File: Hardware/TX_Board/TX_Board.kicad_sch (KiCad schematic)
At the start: 164 parts, among them IC1 QPA9122TR7, IC10 QPA9122TR7, IC11 QPA9122TR7, IC2 MAPS-010164-TR0500, IC3 MAPS-010164-TR0500, IC4 QPA9122TR7, IC5 GP2Y1+, IC6 GP2Y1+, IC7 GP2Y1+, IC8 MAPS-010164-TR0500, IC9 MAPS-010164-TR0500, J1 Conn_Coaxial, J2 Conn_Coaxial, J3 Conn_Coaxial, J4 Conn_Coaxial, U1 SN74HCT138NSR

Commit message: updated logic breakout and added UFL
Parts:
- added C91: 0.1uF, symbol Device:C
- added C92: 100pF, symbol Device:C
- added J5: Conn_02x08_Odd_Even, symbol Connector_Generic:Conn_02x08_Odd_Even
- added L11, L12, L4, L5, L6, L7, L8, L9: U.FL-R-SMT-1_60_, UFLRSMT160, symbol U_FL-R-SMT-1_60_:U.FL-R-SMT-1_60_
- added R48, R49, R50, R51, R52, R53, R54, R55: 0, symbol Device:R_US
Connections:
- net VCC1 is gone; now on net VCC: C38.1, C39.1, C77.1, C78.1, R19.1, R38.1
- net ATTN_LE_1: now also J5.3 (Pin_3), R50.2; no longer U1.14 (Y1)
- net ATTN_LE_2: now also J5.7 (Pin_7), R52.2; no longer U1.12 (Y3)
- net ATTN_LE_3: now also J5.11 (Pin_11), R54.2; no longer U1.10 (Y5)
- net ATTN_LE_4: now also J5.15 (Pin_15), R55.1; no longer U1.7 (Y7)
- net GND: now also C91.1, C92.1, L11.1 (GND_1), L11.2 (GND_2), L12.1 (GND_1), L12.2 (GND_2), L4.1 (GND_1), L4.2 (GND_2), L5.1 (GND_1), L5.2 (GND_2), L6.1 (GND_1), L6.2 (GND_2), L7.1 (GND_1), L7.2 (GND_2), L8.1 (GND_1), L8.2 (GND_2), L9.1 (GND_1), L9.2 (GND_2)
- net PS_LE_1: now also J5.1 (Pin_1), R49.2; no longer U1.15 (Y0)
- net PS_LE_2: now also J5.5 (Pin_5), R51.2; no longer U1.13 (Y2)
- net PS_LE_3: now also J5.9 (Pin_9), R53.2; no longer U1.11 (Y4)
- net PS_LE_4: now also J5.13 (Pin_13), R48.2; no longer U1.9 (Y6)
- net VCC: now also C91.2, C92.2
- net at C76.2, IC11.2 (RFIN): now also L11.3 (SIG)
- net at C14.2, IC1.2 (RFIN): now also L9.3 (SIG)
- net at AT.4 (RFIN), IC2.14 (RF_OUT): now also L4.3 (SIG)
- net at C37.2, IC4.2 (RFIN): now also L8.3 (SIG)
- net at AT3.4 (RFIN), IC9.14 (RF_OUT): now also L6.3 (SIG)
- net at AT2.4 (RFIN), IC8.14 (RF_OUT): now also L7.3 (SIG)
- net at AT1.4 (RFIN), IC3.14 (RF_OUT): now also L5.3 (SIG)
- net at C75.2, IC10.2 (RFIN): now also L12.3 (SIG)
- new net: R55.2, U1.7 (Y7)
- new net: R48.1, U1.9 (Y6)
- new net: R51.1, U1.13 (Y2)
- new net: R54.1, U1.10 (Y5)
- new net: R53.1, U1.11 (Y4)
- new net: R52.1, U1.12 (Y3)
- new net: R50.1, U1.14 (Y1)
- new net: R49.1, U1.15 (Y0)
- no-connect marks 0 -> 13
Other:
- moved on the sheet: AT, AT1, AT2, AT3, C11, C12, C13, C14, C15, C16, C17, C18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

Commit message: updated tx board and started layour
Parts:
- added J10, J7, J8, J9: Conn_01x01_Pin, Connector_PinHeader_2.00mm:PinHeader_1x01_P2.00mm_Vertical, symbol Connector:Conn_01x01_Pin
- added J11: Conn_Coaxial, Connector_Coaxial:SMA_Amphenol_132289_EdgeMount, symbol Connector:Conn_Coaxial
- added J12: Conn_02x04_Odd_Even, Connector_PinHeader_2.00mm:PinHeader_2x04_P2.00mm_Vertical, symbol Connector_Generic:Conn_02x04_Odd_Even
- added J6: Conn_01x03_Socket, Connector_PinSocket_2.00mm:PinSocket_1x03_P2.00mm_Vertical, symbol Connector:Conn_01x03_Socket
- added L13, L14, L15, L16: U.FL-R-SMT-1_60_, UFL_R_SMT1_1_60:UFLRSMT160, symbol U_FL-R-SMT-1_60_:U.FL-R-SMT-1_60_
- added R56, R57: 1M, Resistor_SMD:R_0402_1005Metric, symbol Device:R_US
- added U2: LDO40LPU50RY, Package_DFN_QFN:DFN-6-1EP_3x3mm_P0.95mm_EP1.7x2.6mm, symbol Regulator_Linear:LDO40LPU50RY
- added U3: ADP7182AUJZ-5.0, Package_TO_SOT_SMD:TSOT-23-5, symbol Regulator_Linear:ADP7182AUJZ-5.0
- AT1, AT2, AT3: footprint QFN50P300X300X90-17N -> RFSA3713TR7:QFN50P300X300X90-17N
- AT4: renamed from AT; footprint QFN50P300X300X90-17N -> RFSA3713TR7:QFN50P300X300X90-17N
- C1, C10, C11, C12, C13, C19, C2, C20, C21, C23, C24, C25, C26, C27, C28, C29, C3, C30, C31, C32, C33, C34, C35, C36, C4, C45, C46, C47, C48, C49, C5, C50, C51, C52, C53, C54, C55, C56, C57, C58, C59, C6, C60, C61, C62, C63, C64, C65, C66, C67, C68, C69, C7, C70, C71, C72, C73, C74, C8, C9, C91, C92: footprint (none) -> Capacitor_SMD:C_0402_1005Metric
- IC2, IC3, IC8, IC9: footprint QFN50P400X400X100-25N-D -> MAPS-010164-TR0500:QFN50P400X400X100-25N-D
- IC5, IC6, IC7: footprint QFN51P300X300X89-13N -> GP2Y1+:QFN51P300X300X89-13N
- J5: footprint (none) -> Connector_PinHeader_2.00mm:PinHeader_2x08_P2.00mm_Vertical
- L11, L12, L4, L5, L6, L7, L8, L9: footprint UFLRSMT160 -> UFL_R_SMT1_1_60:UFLRSMT160
- R1, R10, R11, R12, R13, R14, R15, R16, R17, R18, R2, R24, R25, R26, R27, R28, R29, R3, R30, R31, R32, R33, R34, R35, R36, R37, R4, R48, R49, R5, R50, R51, R52, R53, R54, R55: footprint (none) -> Resistor_SMD:R_0402_1005Metric
- U1: footprint NS16 -> SN74HCT138NSR:NS16
- renumbered C14 to C93, C17 to C94, R6 to R58
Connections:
- net ATTN_LE_1: now also J5.4 (Pin_4)
- net ATTN_LE_2: now also J5.8 (Pin_8)
- net ATTN_LE_3: now also J5.12 (Pin_12)
- net ATTN_LE_4: now also J5.16 (Pin_16)
- net GND: now also J11.2 (Ext), J6.2 (Pin_2), L13.1 (GND_1), L13.2 (GND_2), L14.1 (GND_1), L14.2 (GND_2), L15.1 (GND_1), L15.2 (GND_2), L16.1 (GND_1), L16.2 (GND_2), R56.1, R57.1, U2.1 (GND), U2.7 (GND), U3.1 (GND); no longer U1.4 (*G2A), U1.5 (*G2B)
- net GPIO0: now also J12.1 (Pin_1), J12.2 (Pin_2)
- net GPIO1: now also J12.3 (Pin_3), J12.4 (Pin_4)
- net GPIO2: now also J12.5 (Pin_5), J12.6 (Pin_6)
- net GPIO3: now also J12.7 (Pin_7), J12.8 (Pin_8)
- net PS_LE_1: now also J5.2 (Pin_2)
- net PS_LE_2: now also J5.6 (Pin_6)
- net PS_LE_3: now also J5.10 (Pin_10)
- net PS_LE_4: now also J5.14 (Pin_14)
- net RF_IN1: now also L13.3 (SIG)
- net RF_IN2: now also L14.3 (SIG)
- net RF_IN3: now also L16.3 (SIG)
- net RF_IN4: now also L15.3 (SIG)
- net VCC: now also U2.4 (Vout)
- net VEE: now also U3.5 (VOUT)
- net SDR_RF_OUT: no longer names the net of IC5.2 (SUM_PORT)
- net SDR_RF_OUT: now also J11.1 (In)
- new net: R57.2, U1.5 (*G2B)
- new net: R56.2, U1.4 (*G2A)
- new net +VDC: J6.1 (Pin_1), U2.2 (EN), U2.3 (Vin), U3.3 (EN)
- new net -VDC: J6.3 (Pin_3), U3.2 (VIN)
- no-connect marks 13 -> 5
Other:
- moved on the sheet: AT1, AT2, AT3, AT4, C1, C10, C11, C12, C13, C14, C15, C16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

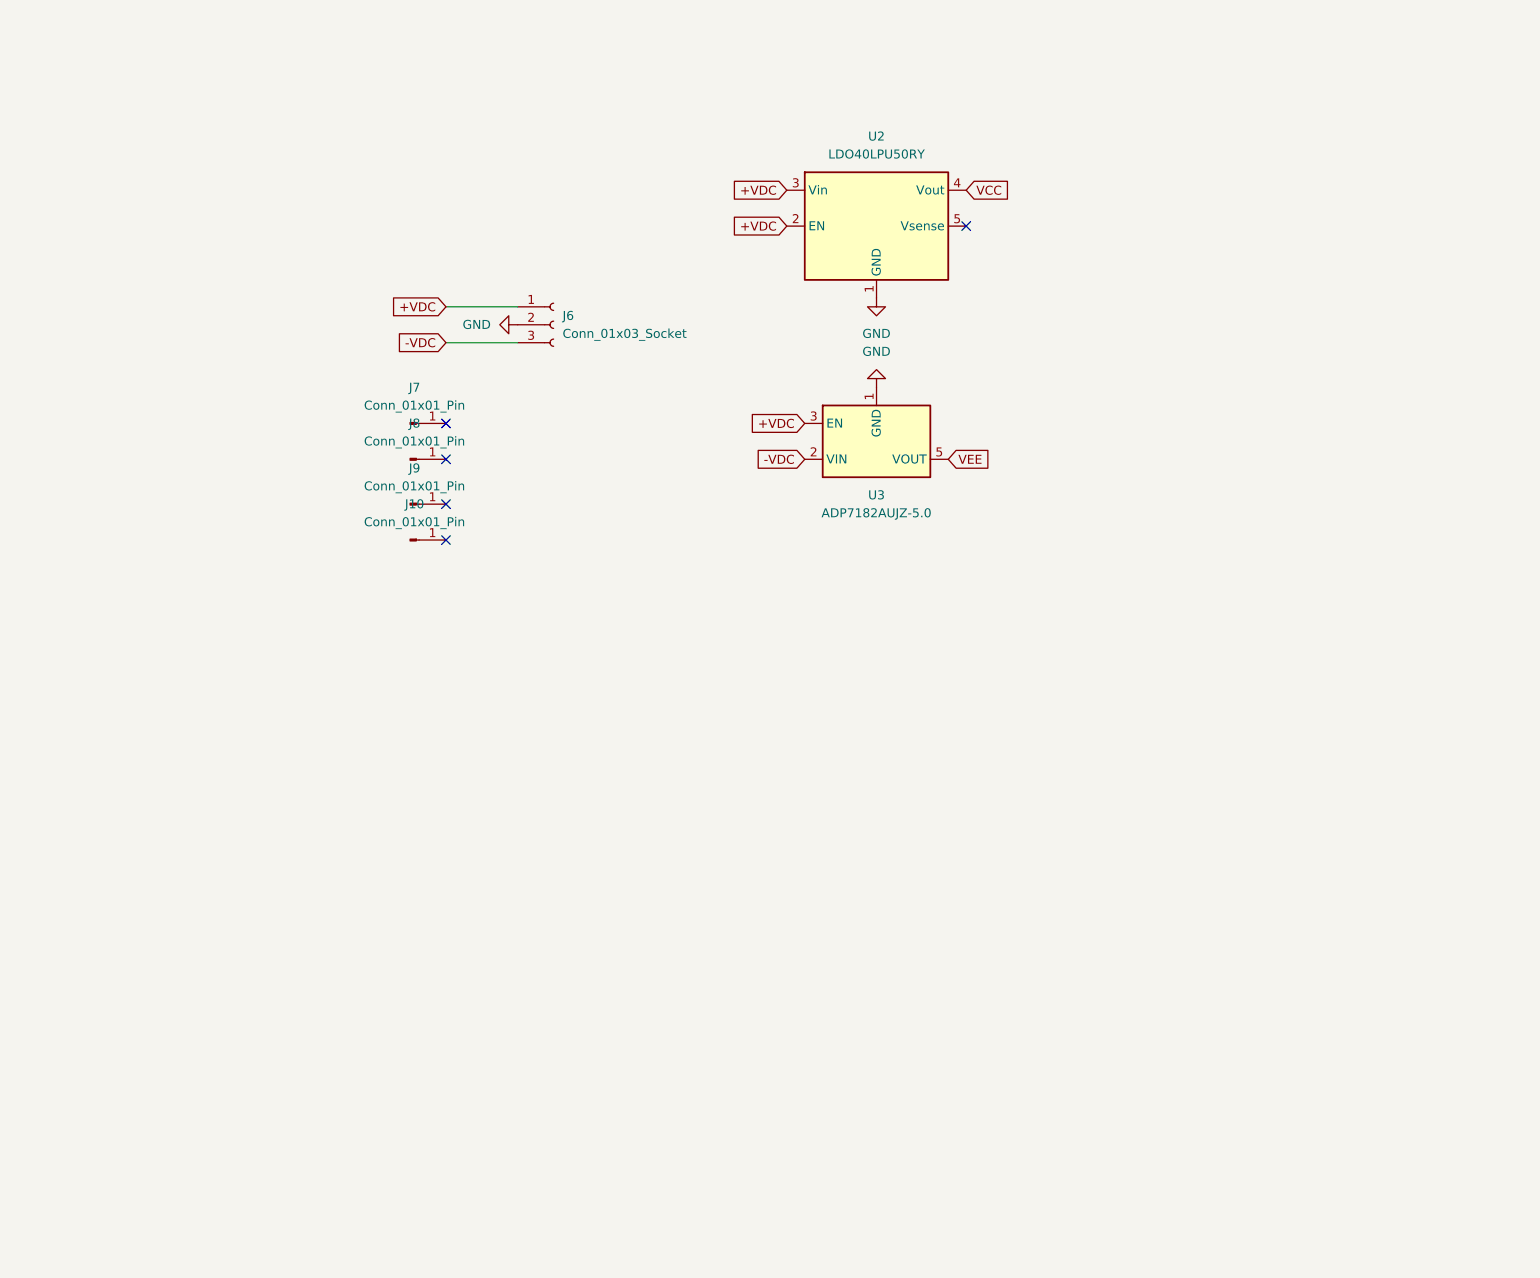
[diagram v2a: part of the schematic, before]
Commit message: added LDO
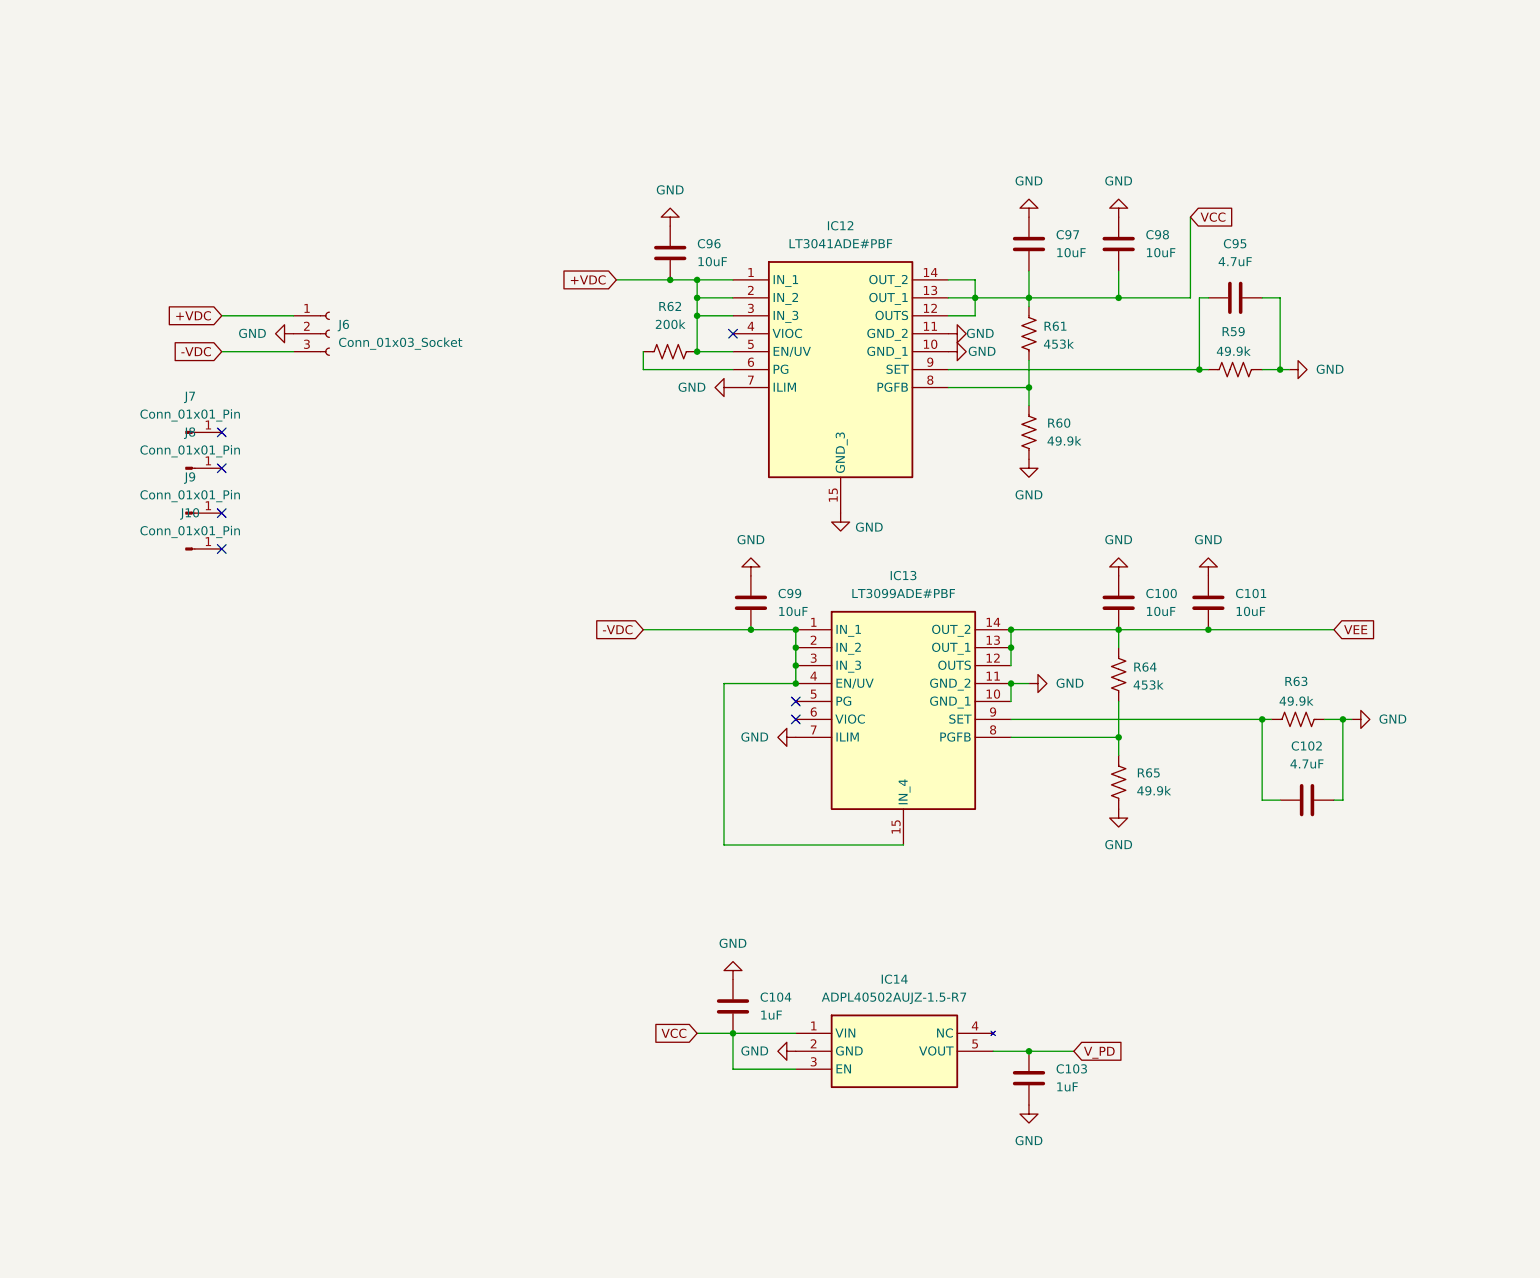
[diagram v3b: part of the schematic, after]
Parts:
- removed U2: LDO40LPU50RY, Package_DFN_QFN:DFN-6-1EP_3x3mm_P0.95mm_EP1.7x2.6mm, symbol Regulator_Linear:LDO40LPU50RY
- removed U3: ADP7182AUJZ-5.0, Package_TO_SOT_SMD:TSOT-23-5, symbol Regulator_Linear:ADP7182AUJZ-5.0
- added C100, C101, C96, C97, C98, C99: 10uF, Capacitor_SMD:C_1206_3216Metric, symbol Device:C
- added C102, C95: 4.7uF, Capacitor_SMD:C_1206_3216Metric, symbol Device:C
- added C103, C104: 1uF, Capacitor_SMD:C_0603_1608Metric, symbol Device:C
- added IC12: LT3041ADE#PBF, LT3041ADE:SON50P300X400X80-15N-D, symbol LT3041ADE#PBF:LT3041ADE#PBF
- added IC13: LT3099ADE#PBF, LT3099ADE:SON50P300X400X80-15N-D, symbol LT3099ADE#PBF:LT3099ADE#PBF
- added IC14: ADPL40502AUJZ-1.5-R7, ADPL40502:SOT95P280X100-5N, symbol ADPL40502AUJZ-1_5-R7:ADPL40502AUJZ-1.5-R7
- added R59, R60, R63, R65: 49.9k, Resistor_SMD:R_0201_0603Metric, symbol Device:R_US
- added R61, R64: 453k, Resistor_SMD:R_0201_0603Metric, symbol Device:R_US
- added R62: 200k, Resistor_SMD:R_0201_0603Metric, symbol Device:R_US
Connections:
- net +VDC: now also C96.2, IC12.1 (IN_1), IC12.2 (IN_2), IC12.3 (IN_3), IC12.5 (EN/UV), R62.2
- net -VDC: now also C99.2, IC13.1 (IN_1), IC13.15 (IN_4), IC13.2 (IN_2), IC13.3 (IN_3), IC13.4 (EN/UV)
- net GND: now also C100.1, C101.1, C102.2, C103.2, C104.1, C95.2, C96.1, C97.1, C98.1, C99.1, IC12.10 (GND_1), IC12.11 (GND_2), IC12.15 (GND_3), IC12.7 (ILIM), IC13.10 (GND_1), IC13.11 (GND_2), IC13.7 (ILIM), IC14.2 (GND), R59.1, R60.2, R63.1, R65.2
- net VCC: now also C104.2, C97.2, C98.2, IC12.12 (OUTS), IC12.13 (OUT_1), IC12.14 (OUT_2), IC14.1 (VIN), IC14.3 (EN), R61.1
- net VEE: now also C100.2, C101.2, IC13.12 (OUTS), IC13.13 (OUT_1), IC13.14 (OUT_2), R64.1
- net V_PD: now also C103.1, IC14.5 (VOUT)
- new net: C102.1, IC13.9 (SET), R63.2
- new net: C95.1, IC12.9 (SET), R59.2
- new net: IC12.6 (PG), R62.1
- new net: IC12.8 (PGFB), R60.1, R61.2
- new net: IC13.8 (PGFB), R64.2, R65.1
- no-connect marks 5 -> 7
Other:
- moved on the sheet: J10, J6, J7, J8, J9

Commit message: switched out UFL to SWG
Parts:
- removed L11, L12, L13, L14, L15, L16, L4, L5, L6, L7, L8, L9: U.FL-R-SMT-1_60_, UFL_R_SMT1_1_60:UFLRSMT160, symbol U_FL-R-SMT-1_60_:U.FL-R-SMT-1_60_
- added J13, J14, J15, J16, J17, J18, J19, J20, J21, J22, J23, J24: MM8030-2610RJ3, MM8030:MM80302610RJ3, symbol MM8030-2610RJ3:MM8030-2610RJ3
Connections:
- net ATTN_LE2 is gone; now on net ATTN_LE_2: R18.2
- net ATTN_LE4 is gone; now on net ATTN_LE_4: R36.2
- net PS_LE2 is gone; now on net PS_LE_2: R14.2
- net PS_LE4 is gone; now on net PS_LE_4: R28.2
- net GND: now also J13.3 (GND_1), J13.4 (GND_2), J14.3 (GND_1), J14.4 (GND_2), J15.3 (GND_1), J15.4 (GND_2), J16.3 (GND_1), J16.4 (GND_2), J17.3 (GND_1), J17.4 (GND_2), J18.3 (GND_1), J18.4 (GND_2), J19.3 (GND_1), J19.4 (GND_2), J20.3 (GND_1), J20.4 (GND_2), J21.3 (GND_1), J21.4 (GND_2), J22.3 (GND_1), J22.4 (GND_2), J23.3 (GND_1), J23.4 (GND_2), J24.3 (GND_1), J24.4 (GND_2)
- net RF_IN1: now also J13.2 (OUT); no longer IC6.9 (PORT_2)
- net RF_IN2: now also J14.2 (OUT); no longer IC6.7 (PORT_1)
- net RF_IN3: now also J15.2 (OUT); no longer IC7.9 (PORT_2)
- net RF_IN4: now also J16.2 (OUT); no longer IC7.7 (PORT_1)
- net at C14.2: now also J18.1 (IN); no longer IC1.2 (RFIN)
- net at IC4.2 (RFIN): now also J20.2 (OUT); no longer C37.2
- net at IC3.14 (RF_OUT): now also J19.1 (IN); no longer AT1.4 (RFIN)
- net at AT2.4 (RFIN): now also J23.2 (OUT); no longer IC8.14 (RF_OUT)
- net at IC11.2 (RFIN): now also J22.2 (OUT); no longer C76.2
- net at AT4.4 (RFIN): now also J17.2 (OUT); no longer IC2.14 (RF_OUT)
- net at AT3.4 (RFIN): now also J21.2 (OUT); no longer IC9.14 (RF_OUT)
- net at C75.2: now also J24.1 (IN); no longer IC10.2 (RFIN)
- new net: IC10.2 (RFIN), J24.2 (OUT)
- new net: IC2.14 (RF_OUT), J17.1 (IN)
- new net: C76.2, J22.1 (IN)
- new net: IC9.14 (RF_OUT), J21.1 (IN)
- new net: IC1.2 (RFIN), J18.2 (OUT)
- new net: C37.2, J20.1 (IN)
- new net: AT1.4 (RFIN), J19.2 (OUT)
- new net: IC6.7 (PORT_1), J14.1 (IN)
- new net: IC6.9 (PORT_2), J13.1 (IN)
- new net: IC7.7 (PORT_1), J16.1 (IN)
- new net: IC7.9 (PORT_2), J15.1 (IN)
- new net: IC8.14 (RF_OUT), J23.1 (IN)
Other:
- moved on the sheet: IC6

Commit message: updated schematics
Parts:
- removed J12: Conn_02x04_Odd_Even, Connector_PinHeader_2.00mm:PinHeader_2x04_P2.00mm_Vertical, symbol Connector_Generic:Conn_02x04_Odd_Even
- added J6: Conn_02x12_Odd_Even, Connector_PinHeader_2.00mm:PinHeader_2x12_P2.00mm_Vertical, symbol Connector_Generic:Conn_02x12_Odd_Even
- renumbered AT2 to AT1, AT1 to AT2, C96 to C1, C101 to C10, C93 to C100, C94 to C101, C44 to C102, C90 to C103, C18 to C104, C95 to C11, C102 to C12, C45 to C13, C21 to C14, C46 to C15, C1 to C16, C47 to C17, C48 to C18, C23 to C19, C104 to C2, C24 to C20, C49 to C21, C50 to C22, C3 to C23, C2 to C24, C51 to C25, C25 to C26, C52 to C27, C4 to C28, C53 to C29, C99 to C3, C26 to C30, C54 to C31, C5 to C32, C55 to C33, C27 to C34, C56 to C35, C57 to C36, C7 to C37, C28 to C38, C58 to C39, C91 to C4, C6 to C40, C59 to C41, C60 to C42, C29 to C43, C30 to C44, C61 to C45, C62 to C46, C9 to C47, C8 to C48, C63 to C49, C92 to C5, C31 to C50, C64 to C51, C10 to C52, C65 to C53, C66 to C54, C32 to C55, C33 to C56, C67 to C57, C68 to C58, C11 to C59, C97 to C6, C12 to C60, C69 to C61, C34 to C62, C70 to C63, C13 to C64, C71 to C65, C35 to C66, C72 to C67, C19 to C68, C73 to C69, C103 to C7, C36 to C70, C74 to C71, C75 to C72, C20 to C73, C37 to C74, C76 to C75, C14 to C76, C38 to C79, C98 to C8, C39 to C80, C79 to C81, C80 to C82, C15 to C83, C16 to C84, C81 to C85, C40 to C86, C82 to C87, C17 to C88, C83 to C89, C100 to C9, C41 to C90, C84 to C91, C22 to C92, C85 to C93, C86 to C94, C42 to C95, C43 to C96, C87 to C97, C88 to C98, C89 to C99, IC5 to IC1, IC2 to IC10, IC10 to IC11, IC4 to IC12, IC11 to IC13, IC1 to IC14, IC7 to IC2, IC6 to IC3, IC12 to IC4, IC13 to IC5, IC14 to IC6, IC8 to IC7, IC3 to IC8, J11 to J1, J14 to J10, J15 to J11, J16 to J12, J19 to J13, J21 to J14, J23 to J15, J17 to J16, J24 to J17, J20 to J18, J22 to J19, J7 to J2, J18 to J20, J3 to J21, J1 to J22, J4 to J23, J2 to J24, J8 to J3, J9 to J4, J10 to J5, J6 to J7, J5 to J8, J13 to J9, L2 to L1, L1 to L2, L10 to L4, R56 to R1, R54 to R10, R48 to R11, R61 to R12, R60 to R13, R64 to R14, R65 to R15, R59 to R16, R63 to R17, R24 to R18, R12 to R19, R57 to R2, R25 to R20, R1 to R21, R26 to R22, R13 to R23, R27 to R24, R28 to R25, R2 to R26, R14 to R27, R29 to R28, R3 to R29, R55 to R3, R15 to R31, R31 to R32, R4 to R33, R32 to R34, R16 to R35, R33 to R36, R5 to R37, R34 to R38, R17 to R39, R62 to R4, R35 to R40, R10 to R41, R36 to R42, R18 to R43, R37 to R44, R11 to R45, R38 to R46, R19 to R47, R39 to R48, R9 to R49, R49 to R5, R40 to R50, R20 to R51, R41 to R52, R58 to R53, R42 to R54, R21 to R55, R43 to R56, R6 to R57, R44 to R58, R22 to R59, R50 to R6, R45 to R60, R7 to R61, R46 to R62, R23 to R63, R47 to R64, R8 to R65, R51 to R7, R52 to R8, R53 to R9
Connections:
- net ATTN_A0_1 is gone; now on net ATTN_A0: AT3.2 (A0), AT4.2 (A0)
- net ATTN_A1_1 is gone; now on net ATTN_A1: AT3.15 (A1), AT4.15 (A1)
- net ATTN_A2_1 is gone; now on net ATTN_A2: AT3.16 (A2), AT4.16 (A2)
- net ATTN_SI_1 is gone; now on net ATTN_SI: R36.1, R37.1
- net SER OUT is gone; now on net PS_SER_OUT: R30.1, R31.1
- net ATTN_A0: now also J6.19 (Pin_19), J6.20 (Pin_20)
- net ATTN_A1: now also J6.21 (Pin_21), J6.22 (Pin_22)
- net ATTN_A2: now also J6.23 (Pin_23), J6.24 (Pin_24)
- net ATTN_CLK: now also J6.17 (Pin_17), J6.18 (Pin_18)
- net ATTN_SI: now also J6.15 (Pin_15), J6.16 (Pin_16)
- net GPIO0: now also J6.1 (Pin_1), J6.2 (Pin_2)
- net GPIO1: now also J6.3 (Pin_3), J6.4 (Pin_4)
- net GPIO2: now also J6.5 (Pin_5), J6.6 (Pin_6)
- net GPIO3: now also J6.7 (Pin_7), J6.8 (Pin_8)
- net PS_CLK: now also J6.11 (Pin_11), J6.12 (Pin_12)
- net PS_SER_IN: now also J6.10 (Pin_10), J6.9 (Pin_9)
- net PS_SER_OUT: now also J6.13 (Pin_13), J6.14 (Pin_14)
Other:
- note added: "+5V, -5V, 1.8V Power Source from LDO"
- note added: "Digital Logic Decoder"
- note added: "Power Board Adaptor"

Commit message: refactored pcb
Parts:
- removed AT1, AT2, AT3, AT4: RFSA3713TR7, RFSA3713TR7:QFN50P300X300X90-17N, symbol RFSA3713TR7:RFSA3713TR7
- removed C100, C78, C80, C82, C84, C93, C95, C97: 1 uF, Capacitor_SMD:C_0402_1005Metric, symbol Device:C
- removed C101, C77, C79, C81, C83, C85, C86, C87, C88, C89, C90, C91, C92, C94, C96, C98: 100 pF, Capacitor_SMD:C_0402_1005Metric, symbol Device:C
- removed C102, C103, C104, C72, C74, C75, C76, C99: 18 pF, Capacitor_SMD:C_0402_1005Metric, symbol Device:C
- removed C13, C14, C15, C16, C17, C19, C21, C23, C41, C43, C45, C47: 0.1uF, Capacitor_SMD:C_0402_1005Metric, symbol Device:C
- removed C18, C20, C22, C24, C25, C26, C27, C28, C42, C44, C46, C48: 100pF, Capacitor_SMD:C_0402_1005Metric, symbol Device:C
- removed C29, C30, C31, C32, C33, C34, C35, C36, C37, C38, C39, C40, C49, C50, C51, C52, C61, C62, C63, C64, C65, C66, C67, C68, C69, C70, C71, C73: 300pF, Capacitor_SMD:C_0402_1005Metric, symbol Device:C
- removed C53, C55, C57, C59: 470p, Capacitor_SMD:C_0402_1005Metric, symbol Device:C
- removed C54, C56, C58, C60: 1uF, Capacitor_SMD:C_0402_1005Metric, symbol Device:C
- removed IC10, IC7, IC8, IC9: MAPS-010164-TR0500, MAPS-010164-TR0500:QFN50P400X400X100-25N-D, symbol MAPS-010164-TR0500:MAPS-010164-TR0500
- removed IC11, IC12, IC13, IC14: QPA9122TR7, QPA9122TR7:QPA9122TR7, symbol QPA9122TR7:QPA9122TR7
- removed J13, J14, J15, J16, J17, J18, J19, J20: MM8030-2610RJ3, MM8030:MM80302610RJ3, symbol MM8030-2610RJ3:MM8030-2610RJ3
- removed J21, J22, J23, J24: Conn_Coaxial, Connector_Coaxial:SMA_Amphenol_132289_EdgeMount, symbol Connector:Conn_Coaxial
- removed L1, L2, L3, L4: 12 nH, Inductor_SMD:L_0402_1005Metric, symbol Device:L
- removed R18, R19, R20, R21, R22, R23, R24, R25, R26, R27, R28, R29, R30, R31, R32, R33, R34, R35, R36, R37, R38, R39, R40, R41, R42, R43, R44, R45: 10, Resistor_SMD:R_0402_1005Metric, symbol Device:R_US
- removed R46, R47, R48, R49: 8.2, Resistor_SMD:R_0402_1005Metric, symbol Device:R_US
- removed R50, R51, R52, R53, R58, R59, R60, R61, R62, R63, R64, R65: 0, Resistor_SMD:R_0402_1005Metric, symbol Device:R_US
- removed R54, R55, R56, R57: 51, Resistor_SMD:R_0402_1005Metric, symbol Device:R_US
- C1, C10, C11, C12, C2, C3, C4, C5, C6, C7, C8, C9: symbol Device:C -> tx_board_symbol_library:C
- IC1, IC2, IC3: footprint GP2Y1+:QFN51P300X300X89-13N -> tx_board_footprints:QFN51P300X300X89-13N; symbol GP2Y1+:GP2Y1+ -> tx_board_symbol_library:GP2Y1+
- IC4: footprint LT3041ADE:SON50P300X400X80-15N-D -> tx_board_footprints:SON50P300X400X80-15N-D; symbol LT3041ADE#PBF:LT3041ADE#PBF -> tx_board_symbol_library:LT3041ADE#PBF
- IC5: footprint LT3099ADE:SON50P300X400X80-15N-D -> tx_board_footprints:SON50P300X400X80-15N-D; symbol LT3099ADE#PBF:LT3099ADE#PBF -> tx_board_symbol_library:LT3099ADE#PBF
- IC6: footprint ADPL40502:SOT95P280X100-5N -> tx_board_footprints:SOT95P280X100-5N; symbol ADPL40502AUJZ-1_5-R7:ADPL40502AUJZ-1.5-R7 -> tx_board_symbol_library:ADPL40502AUJZ-1.5-R7
- J1: symbol Connector:Conn_Coaxial -> tx_board_symbol_library:Conn_Coaxial
- J10, J11, J12, J9: footprint MM8030:MM80302610RJ3 -> tx_board_footprints:MM80302610RJ3; symbol MM8030-2610RJ3:MM8030-2610RJ3 -> tx_board_symbol_library:MM8030-2610RJ3
- J2, J3, J4, J5: symbol Connector:Conn_01x01_Pin -> tx_board_symbol_library:Conn_01x01_Pin
- J6: symbol Connector_Generic:Conn_02x12_Odd_Even -> tx_board_symbol_library:Conn_02x12_Odd_Even
- J7: symbol Connector:Conn_01x03_Socket -> tx_board_symbol_library:Conn_01x03_Socket
- J8: symbol Connector_Generic:Conn_02x08_Odd_Even -> tx_board_symbol_library:Conn_02x08_Odd_Even
- R1, R10, R11, R12, R13, R14, R15, R16, R17, R2, R3, R4, R5, R6, R7, R8, R9: symbol Device:R_US -> tx_board_symbol_library:R_US
- U1: footprint SN74HCT138NSR:NS16 -> tx_board_footprints:NS16; symbol SN74HCT138NSR:SN74HCT138NSR -> tx_board_symbol_library:SN74HCT138NSR
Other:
- added sheet TX_Channel0 (untitled.kicad_sch)
- added sheet TX_Channel1 (untitled.kicad_sch)
- added sheet TX_Channel2 (untitled.kicad_sch)
- added sheet TX_Channel3 (untitled.kicad_sch)
